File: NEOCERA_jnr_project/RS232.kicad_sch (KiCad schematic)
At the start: 12 parts, among them U1 ICL3232, U2 ICL3232

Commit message: changes
edited symbols and usb schematic
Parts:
- U1, U2: footprint Package_SO:SOIC-16W_7.5x12.8mm_P1.27mm -> Package_SO:SOIC-16_3.9x9.9mm_P1.27mm
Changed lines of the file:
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@@
 			)
 		)
-		(property "Footprint" "Package_SO:SOIC-16W_7.5x12.8mm_P1.27mm"
+		(property "Footprint" "Package_SO:SOIC-16_3.9x9.9mm_P1.27mm"
 			(at 181.61 130.81 0)
 			(effects
@@
 			)
 		)
-		(property "Footprint" "Package_SO:SOIC-16W_7.5x12.8mm_P1.27mm"
+		(property "Footprint" "Package_SO:SOIC-16_3.9x9.9mm_P1.27mm"
 			(at 72.39 130.81 0)
 			(effects

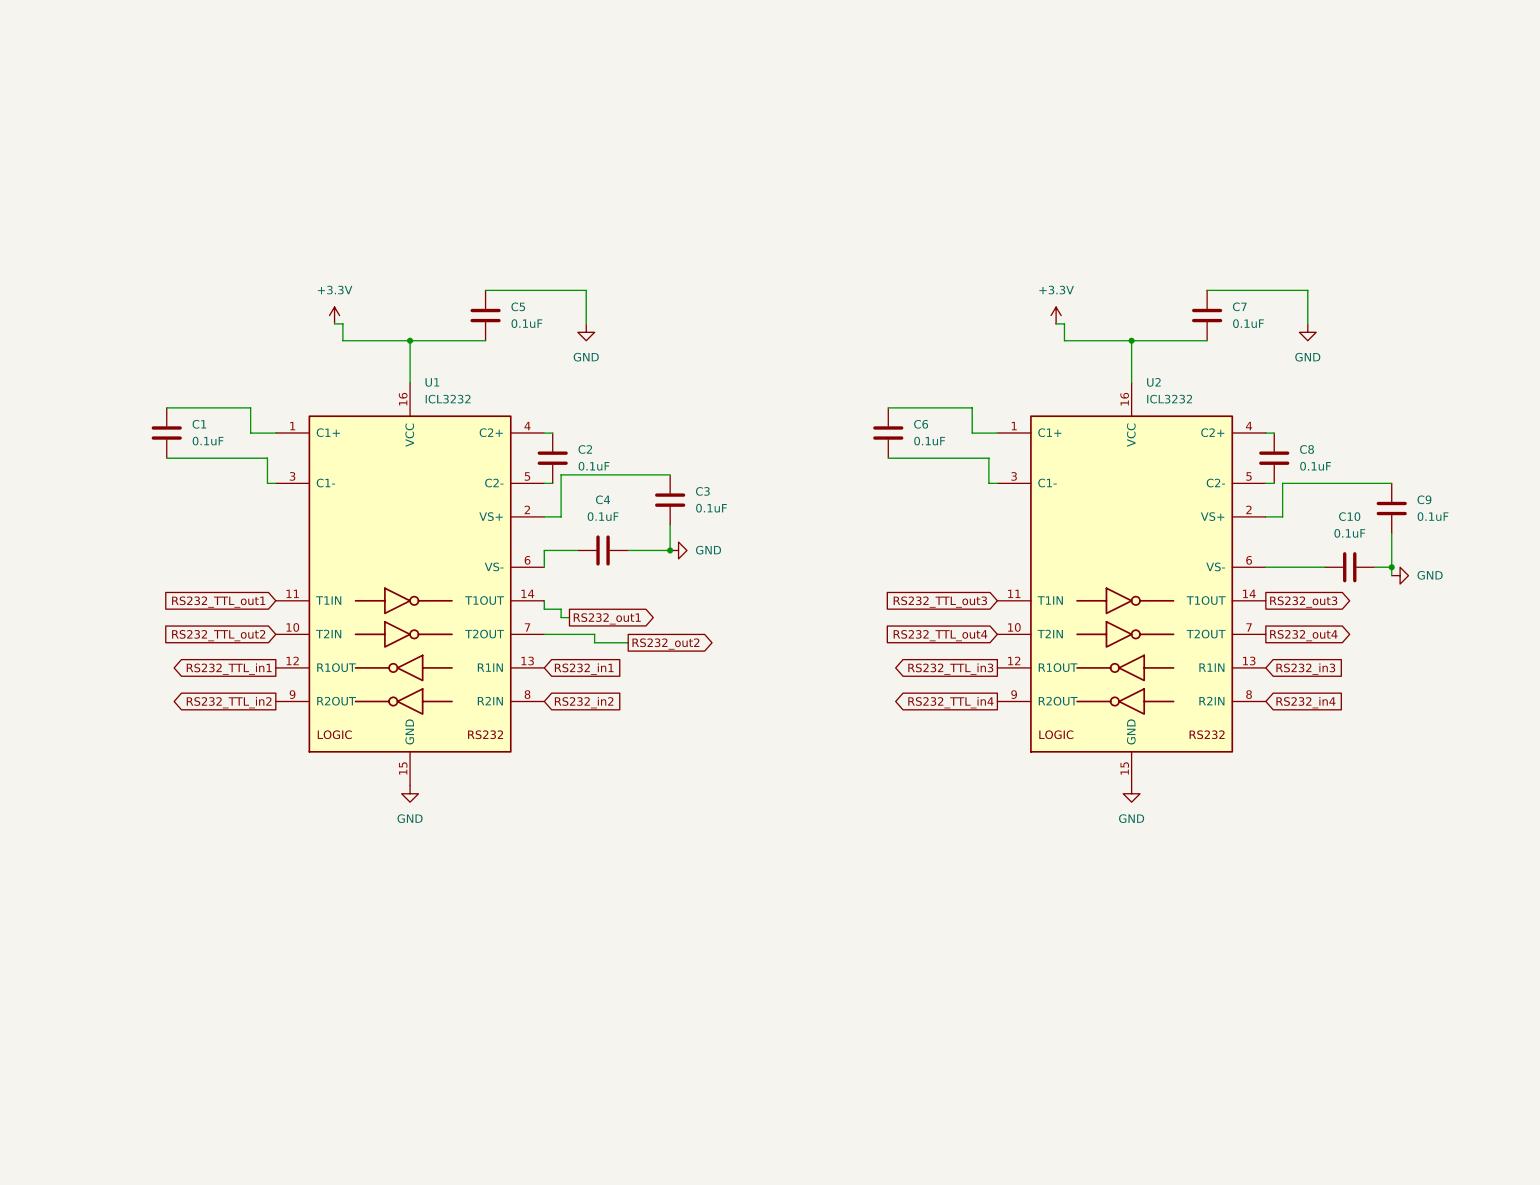
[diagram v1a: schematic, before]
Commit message: Edits made with Dr. Caw.
I added the net to the root
I added the write global nets to some of the previously designed symbols like TX/RX
I added a 3.3V pullup resistor to the opto
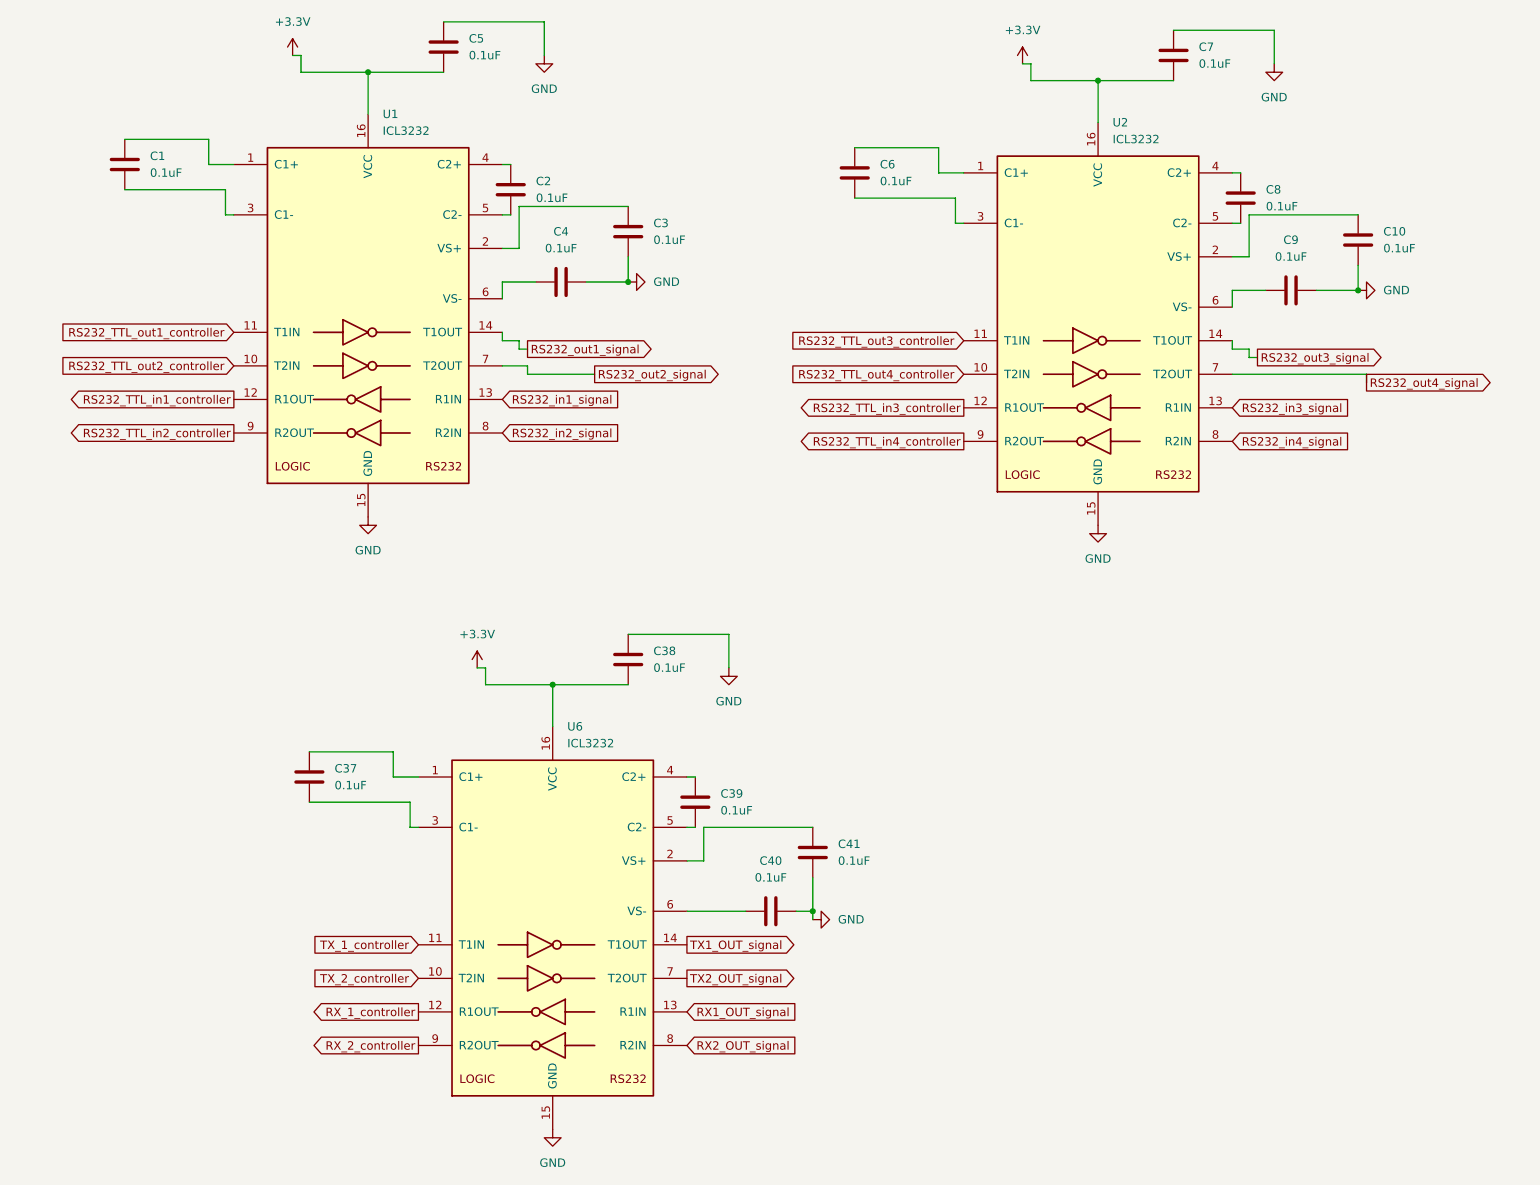
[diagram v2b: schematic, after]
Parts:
- added C37, C38, C39, C40, C41: 0.1uF, Capacitor_SMD:C_0603_1608Metric_Pad1.08x0.95mm_HandSolder, symbol Device:C
- added U6: ICL3232, Package_SO:SOIC-16_3.9x9.9mm_P1.27mm, symbol Interface_UART:ICL3232
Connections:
- net +3.3V: now also C38.2, U6.16 (VCC)
- net GND: now also C38.1, C40.2, C41.2, U6.15 (GND)
- net at U2.2 (VS+): now also C10.1; no longer C9.1
- net at U2.6 (VS-): now also C9.1; no longer C10.1
- net RS232_TTL_in1 renamed RS232_TTL_in1_controller
- net RS232_TTL_in2 renamed RS232_TTL_in2_controller
- net RS232_TTL_in3 renamed RS232_TTL_in3_controller
- net RS232_TTL_in4 renamed RS232_TTL_in4_controller
- net RS232_TTL_out1 renamed RS232_TTL_out1_controller 
- net RS232_TTL_out2 renamed RS232_TTL_out2_controller
- net RS232_TTL_out3 renamed RS232_TTL_out3_controller 
- net RS232_TTL_out4 renamed RS232_TTL_out4_controller
- net RS232_in1 renamed RS232_in1_signal
- net RS232_in2 renamed RS232_in2_signal
- net RS232_in3 renamed RS232_in3_signal
- net RS232_in4 renamed RS232_in4_signal
- net RS232_out1 renamed RS232_out1_signal
- net RS232_out2 renamed RS232_out2_signal
- net RS232_out3 renamed RS232_out3_signal
- net RS232_out4 renamed RS232_out4_signal
- new net: C41.1, U6.2 (VS+)
- new net: C37.1, U6.1 (C1+)
- new net: C37.2, U6.3 (C1-)
- new net: C40.1, U6.6 (VS-)
- new net: C39.1, U6.4 (C2+)
- new net: C39.2, U6.5 (C2-)
- new net RX1_OUT_signal: U6.13 (R1IN)
- new net RX2_OUT_signal: U6.8 (R2IN)
- new net RX_1_controller: U6.12 (R1OUT)
- new net RX_2_controller: U6.9 (R2OUT)
- new net TX1_OUT_signal: U6.14 (T1OUT)
- new net TX2_OUT_signal: U6.7 (T2OUT)
- new net TX_1_controller: U6.11 (T1IN)
- new net TX_2_controller: U6.10 (T2IN)
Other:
- moved on the sheet: C1, C2, C3, C4, C5, U1
